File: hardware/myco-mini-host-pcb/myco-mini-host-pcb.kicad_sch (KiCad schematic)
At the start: 38 parts, among them J1 Conn_01x17_Female, J2 Conn_01x17_Female, Q1 AO3401A, Q2 AO3401A, Q3 AO3401A, Q4 AO3401A, SW1 DM-04-V, SW2 TS-1187A-B-A-B, U1 XC9145B33CMR-G, U2 SHT41-AD1B-R2, U3 BH1750FVI-TR, U4 MAX40203AUK+T

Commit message: refactor: echange P1.12/P1.13 entre SENSOR_EN et BAT_SENSE
- SENSOR_EN : P1.12 (J1 pin5) -> P1.13 (J1 pin6)
- BAT_SENSE : P1.13 (J1 pin6) -> P1.12 (J1 pin5)

Verifie avant application : P1.12 = AIN5 et P1.13 = AIN6 dans les tables de
brochage du datasheet nRF54L15, donc les deux broches sont capables SAADC.
L'echange est valide dans les deux sens - BAT_SENSE garde une entree
analogique reelle sur P1.12, et SENSOR_EN n'a besoin que d'un GPIO general.

Nets renommes en consequence (P1_12_SENSOR_EN -> P1_13_SENSOR_EN,
P1_13_BAT_SENSE -> P1_12_BAT_SENSE), plus les notes de Q3/Q4 et la BOM.

Alignement des textes preserve : diff UUID sur les 79 labels, zero
deplacement (7 renommages voulus). ERC inchange a 69.

Co-Authored-By: Claude Sonnet 5 <noreply@anthropic.com>
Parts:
- Q3: Note Sensor VCC switch (BH1750+SHT41+their I2C pull-ups): S=VOUT_3V3 D=SENSOR_3V3 G=P1_12_SENSOR_EN. Added when nRF54 moved onto VOUT_3V3 (was VDD_NRF direct-battery) - sensors need their own switch now to still power down in deep sleep. R1/R2 (I2C pull-ups) moved to SENSOR_3V3 too, so an unpowered sensor isn't backfed through its own SDA/SCL ESD clamps. -> Sensor VCC switch (BH1750+SHT41+their I2C pull-ups): S=VOUT_3V3 D=SENSOR_3V3 G=P1_13_SENSOR_EN. Added when nRF54 moved onto VOUT_3V3 (was VDD_NRF direct-battery) - sensors need their own switch now to still power down in deep sleep. R1/R2 (I2C pull-ups) moved to SENSOR_3V3 too, so an unpowered sensor isn't backfed through its own SDA/SCL ESD clamps.
- Q4: Note Battery-sense divider switch: S=BAT_RAW D=BAT_SENSE_TOP G=P1_12_SENSOR_EN (shared with Q3). Keeps the R11/R12 divider disconnected from BAT_RAW except during the brief active-measurement window, avoiding a continuous leakage path now that the free internal-VDD SAADC battery trick no longer works (VDD_NRF is regulated 3.3V post-merge, not the raw cell). -> Battery-sense divider switch: S=BAT_RAW D=BAT_SENSE_TOP G=P1_13_SENSOR_EN (shared with Q3). Keeps the R11/R12 divider disconnected from BAT_RAW except during the brief active-measurement window, avoiding a continuous leakage path now that the free internal-VDD SAADC battery trick no longer works (VDD_NRF is regulated 3.3V post-merge, not the raw cell).
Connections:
- net P1_12_SENSOR_EN renamed P1_13_SENSOR_EN
- net P1_13_SENSOR_EN: now also J1.6 (Pin_6); no longer J1.5 (Pin_5)
- net P1_13_BAT_SENSE renamed P1_12_BAT_SENSE
- net P1_12_BAT_SENSE: now also J1.5 (Pin_5); no longer J1.6 (Pin_6)
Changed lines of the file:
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@@
 		)
 	)
-	(label "P1_12_SENSOR_EN"
+	(label "P1_13_SENSOR_EN"
 		(at 387.35 90.17 0)
 		(effects
@@
 		)
 	)
-	(label "P1_13_BAT_SENSE"
+	(label "P1_12_BAT_SENSE"
 		(at 412.75 121.92 0)
 		(effects
@@
 		)
 	)
-	(label "P1_13_BAT_SENSE"
+	(label "P1_12_BAT_SENSE"
 		(at 412.75 127 0)
 		(effects
@@
 		)
 	)
-	(label "P1_13_BAT_SENSE"
+	(label "P1_13_SENSOR_EN"
 		(at 46.99 179.07 0)
 		(effects
@@
 		)
 	)
-	(label "P1_12_SENSOR_EN"
+	(label "P1_12_BAT_SENSE"
 		(at 46.99 176.53 0)
 		(effects
@@
 		)
 	)
-	(label "P1_12_SENSOR_EN"
+	(label "P1_13_SENSOR_EN"
 		(at 386.08 44.45 0)
 		(effects
@@
 		)
 	)
-	(label "P1_12_SENSOR_EN"
+	(label "P1_13_SENSOR_EN"
 		(at 264.16 87.63 0)
 		(effects
@@
 			)
 		)
-		(property "Note" "Battery-sense divider switch: S=BAT_RAW D=BAT_SENSE_TOP G=P1_12_SENSOR_EN (shared with Q3). Keeps the R11/R12 divider disconnected from BAT_RAW except during the brief active-measurement window, avoiding a continuous leakage path now that the free internal-VDD SAADC battery trick no longer works (VDD_NRF is regulated 3.3V post-merge, not the raw cell)."
+		(property "Note" "Battery-sense divider switch: S=BAT_RAW D=BAT_SENSE_TOP G=P1_13_SENSOR_EN (shared with Q3). Keeps the R11/R12 divider disconnected from BAT_RAW except during the brief active-measurement window, avoiding a continuous leakage path now that the free internal-VDD SAADC battery trick no longer works (VDD_NRF is regulated 3.3V post-merge, not the raw cell)."
 			(at 410.21 90.17 0)
 			(hide yes)
@@
 			)
 		)
-		(property "Note" "Sensor VCC switch (BH1750+SHT41+their I2C pull-ups): S=VOUT_3V3 D=SENSOR_3V3 G=P1_12_SENSOR_EN. Added when nRF54 moved onto VOUT_3V3 (was VDD_NRF direct-battery) - sensors need their own switch now to still power down in deep sleep. R1/R2 (I2C pull-ups) moved to SENSOR_3V3 too, so an unpowered sensor isn't backfed through its own SDA/SCL ESD clamps."
+		(property "Note" "Sensor VCC switch (BH1750+SHT41+their I2C pull-ups): S=VOUT_3V3 D=SENSOR_3V3 G=P1_13_SENSOR_EN. Added when nRF54 moved onto VOUT_3V3 (was VDD_NRF direct-battery) - sensors need their own switch now to still power down in deep sleep. R1/R2 (I2C pull-ups) moved to SENSOR_3V3 too, so an unpowered sensor isn't backfed through its own SDA/SCL ESD clamps."
 			(at 410.21 44.45 0)
 			(hide yes)

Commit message: feat: C6 (100uF) passe de 0805 a 1206 - moins cher et moins de derating
Le 100uF n'existe qu'en 6.3V en boitier 0805, ce qui en faisait le 3e
composant le plus cher de la carte ($0.63, C141660) pour une capacite
effective fortement reduite par le derating DC bias a 3.3V.

En 1206 : GRM31CR61A107ME05L (Murata, C312983) a $0.3505 (MOQ 5, 81k en
stock) et surtout en 10V au lieu de 6.3V, donc bien moins de derating a
3.3V - on paie moins cher pour plus de capacite reelle.

Empreinte du schema passee a Capacitor_SMD:C_1206_3216Metric (verifie que
les autres condensateurs 0805 ne sont pas affectes). Placement PCB a faire
par l'utilisateur, qui a confirme qu'il y a la place a l'emplacement actuel.

Passifs + inductance : $1.19 -> $0.91/carte.

Co-Authored-By: Claude Sonnet 5 <noreply@anthropic.com>
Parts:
- C6: footprint Capacitor_SMD:C_0805_2012Metric -> Capacitor_SMD:C_1206_3216Metric
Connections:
- no-connect marks 19 -> 21
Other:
- moved on the sheet: SW1

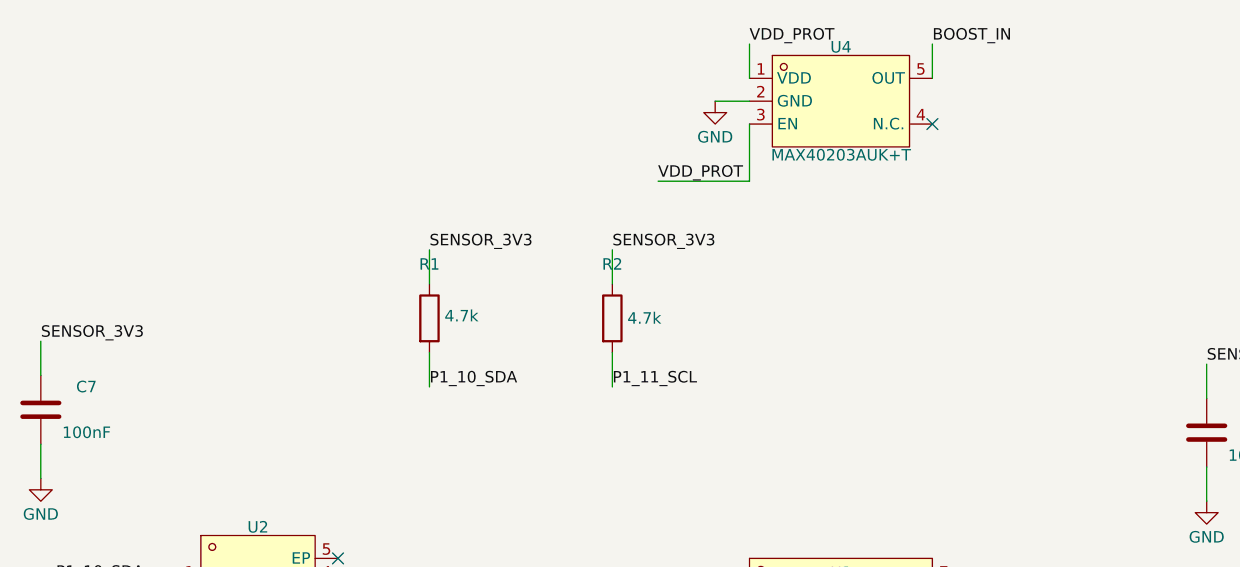
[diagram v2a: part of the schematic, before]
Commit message: fix: types electriques des broches des symboles custom - ERC 56 -> 6
easyeda2kicad laisse toutes les broches en 'unspecified', ce qui rendait
l'ERC inexploitable : 50 des 56 remontees (89%) etaient des avertissements
de compatibilite de types, aucun ne correspondant a un vrai defaut. Un vrai
avertissement pouvait s'y perdre.

Broches typees dans la librairie ET dans le cache lib_symbols du schema
(les deux doivent concorder) :
  power_in      VDD/VCC/VSS/GND/BAT
  power_out     VOUT (U1), OUT (U4)
  input         CE, EN, ADDR, DVI, SCL
  bidirectional SDA
  passive       MOSFET, LED, interrupteurs, sonde sol, pads thermiques, LX

Deux PWR_FLAG ajoutes (#FLG02 sur SENSOR_3V3, #FLG03 sur VDD_PROT) : ces
rails sont alimentes a travers un MOSFET, dont les broches sont 'passive',
donc KiCad n'y voyait aucune source et signalait 'Input Power pin not driven'.
Reference masquee sur les deux (convention, et evite un chevauchement de
texte avec les labels).

Bug corrige en cours de route : la premiere version du script ne
reinitialisait pas le symbole courant en entrant dans un symbole hors table,
et a donc retype les broches de power:GND, power:PWR_FLAG et Device:R/C -
16 erreurs 'Pin not connected' sont apparues. Detecte par l'ERC, restaure
depuis snapshot, corrige, verifie que les symboles stock gardent bien
power_in / power_out / passive.

Resultat : ERC 56 -> 6, dont ZERO erreur. Restent 3 off-grid (edition
manuelle de la zone SW1) et 3 'doesn't match copy in library' (cosmetique,
disparait via 'Update Symbol from Library' dans KiCad).

Connectivite verifiee identique net par net (hors les 2 PWR_FLAG).
Alignement des textes preserve : diff UUID sur 79 labels, zero deplacement.

Co-Authored-By: Claude Sonnet 5 <noreply@anthropic.com>
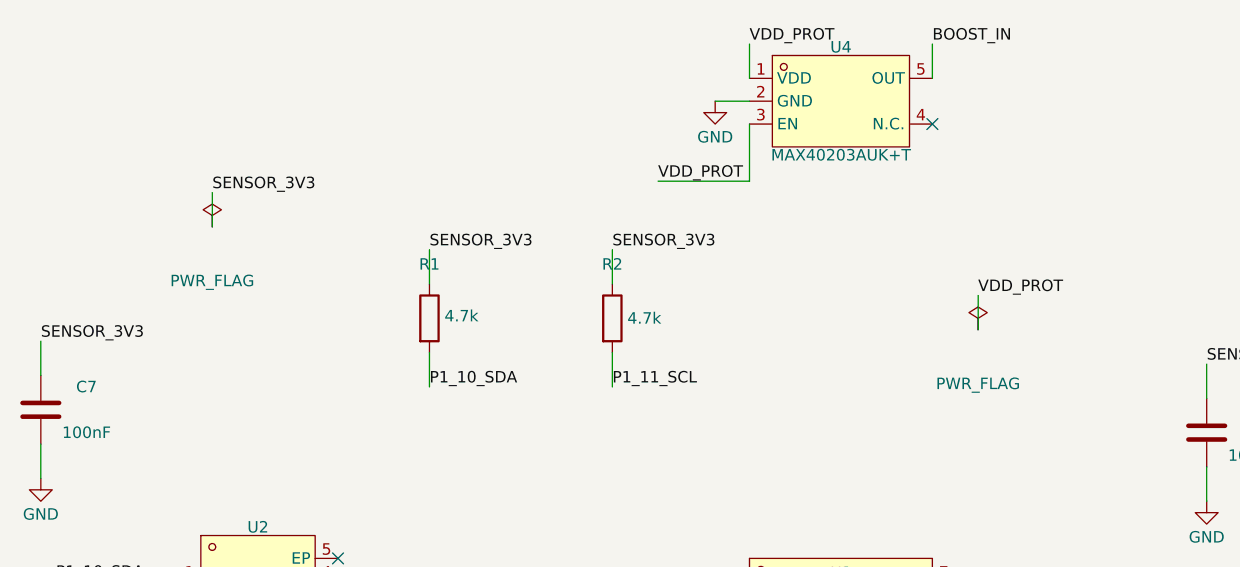
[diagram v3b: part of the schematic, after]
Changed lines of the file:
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@@
 	(wire
 		(pts
-			(xy 97.79 129.54) (xy 101.6 129.54)
-		)
-		(stroke
-			(width 0)
-			(type default)
-		)
-	)
-	(wire
-		(pts
 			(xy 337.82 217.17) (xy 341.63 217.17)
 		)
@@
 		)
 	)
+	(wire
+		(pts
+			(xy 97.79 129.54) (xy 101.6 129.54)
+		)
+		(stroke
+			(width 0)
+			(type default)
+		)
+	)
+	(wire
+		(pts
+			(xy 105.41 90.17) (xy 105.41 86.36)
+		)
+		(stroke
+			(width 0)
+			(type default)
+		)
+	)
+	(wire
+		(pts
+			(xy 190.5 101.6) (xy 190.5 97.78999999999999)
+		)
+		(stroke
+			(width 0)
+			(type default)
+		)
+	)
 	(label "SENSOR_3V3"
 		(at 129.54 92.71 0)
@@
 		)
 	)
+	(label "SENSOR_3V3"
+		(at 105.41 86.36 0)
+		(effects
+			(font
+				(size 1.27 1.27)
+			)
+			(justify left bottom)
+		)
+	)
+	(label "VDD_PROT"
+		(at 190.5 97.78999999999999 0)
+		(effects
+			(font
+				(size 1.27 1.27)
+			)
+			(justify left bottom)
+		)
+	)
 	(symbol
 		(lib_id "power:GND")
@@
 					(unit 1)
 				)
+			)
+		)
+	)
+	(symbol
+		(lib_id "power:PWR_FLAG")
+		(at 105.41 90.17 0)
+		(unit 1)
+		(body_style 1)
+		(exclude_from_sim no)
+		(in_bom no)
+		(on_board yes)
+		(in_pos_files yes)
+		(dnp no)
+		(property "Reference" "#FLG02"
+			(at 105.41 84.17 0)
+			(hide yes)
+			(show_name no)
+			(do_not_autoplace no)
+			(effects
+				(font
+					(size 1.27 1.27)
+				)
+			)
+		)
+		(property "Value" "PWR_FLAG"
+			(at 105.41 96.17 0)
+			(show_name no)
+			(do_not_autoplace no)
+			(effects
+				(font
+					(size 1.27 1.27)
+				)
+			)
+		)
+		(property "Footprint" ""
+			(at 105.41 90.17 0)
+			(hide yes)
+			(show_name no)
+			(do_not_autoplace no)
+			(effects
+				(font
+					(size 1.27 1.27)
+				)
+			)
+		)
+		(property "Datasheet" ""
+			(at 105.41 90.17 0)
+			(show_name no)
+			(do_not_autoplace no)
+			(effects
+				(font
+					(size 1.27 1.27)
+				)
+			)
+		)
+		(property "Description" ""
+			(at 105.41 90.17 0)
+			(show_name no)
+			(do_not_autoplace no)
+			(effects
+				(font
+					(size 1.27 1.27)
+				)
+			)
+		)
+		(pin "1"
+		)
+		(instances
+			(project "myco-mini-host-pcb"
+				(path "/b1969cb4-f84b-4d7e-8508-ab863aa656b2"
+					(reference "#FLG02")
+					(unit 1)
+				)
+			)
+		)
+	)
+	(symbol
+		(lib_id "power:PWR_FLAG")
+		(at 190.5 101.6 0)
+		(unit 1)
+		(body_style 1)
+		(exclude_from_sim no)
+		(in_bom no)
+		(on_board yes)
+		(in_pos_files yes)
+		(dnp no)
+		(property "Reference" "#FLG03"
+			(at 190.5 95.6 0)
+			(hide yes)
+			(show_name no)
+			(do_not_autoplace no)
+			(effects
+				(font
+					(size 1.27 1.27)
+				)
+			)
+		)
+		(property "Value" "PWR_FLAG"
+			(at 190.5 107.6 0)
+			(show_name no)
+			(do_not_autoplace no)
+			(effects
+				(font
+					(size 1.27 1.27)
+				)
+			)
+		)
+		(property "Footprint" ""
+			(at 190.5 101.6 0)
+			(hide yes)
+			(show_name no)
+			(do_not_autoplace no)
+			(effects
+				(font
+					(size 1.27 1.27)
+				)
+			)
+		)
+		(property "Datasheet" ""
+			(at 190.5 101.6 0)
+			(show_name no)
+			(do_not_autoplace no)
+			(effects
+				(font
+					(size 1.27 1.27)
+				)
+			)
+		)
+		(property "Description" ""
+			(at 190.5 101.6 0)
+			(show_name no)
+			(do_not_autoplace no)
+			(effects
+				(font
+					(size 1.27 1.27)
+				)
+			)
+		)
+		(pin "1"
+		)
+		(instances
+			(project "myco-mini-host-pcb"
+				(path "/b1969cb4-f84b-4d7e-8508-ab863aa656b2"
+					(reference "#FLG03")
+					(unit 1)
+				)

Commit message: feat: v1.0.0 - host PCB routé, DRC clean, prêt fab JLCPCB
- Routage complet par l'utilisateur (placement, guard zone soil probe,
  teardrops, trou de fixation gauche)
- Corrections issues de la review Opus 5 finale : dimensions du slit
  d'isolation thermique U2 mises à la spec (1.05mm uniforme sur les
  3 bras), pastilles paste/mask retirées sur U2 (SHT40) et U3 (BH1750)
  pour leurs pads die-exposée, resync librairie<->instances PCB
  (SW1 modèle 3D, BT1 attr smd, courtoisies F.CrtYd manquantes sur
  SW1/SW2/U4)
- 3 vias de la sonde sol passés en plugged+capped (IPC-4761)
- BOM : références LCSC vérifiées et prix réels pour tous les passifs
- DRC final : 0 violation, 0 unconnected
- Ajout docs/cost-tracking.md (suivi des coûts réels host PCB +
  breakout + composants, synchronisé sur le wiki GitHub)
- Datasheets BH1750 et Sensirion (SHT4x) ajoutés à misc/
- .gitignore : exclusion des exports générés (gerbers JLCPCB, rendus
  SVG temporaires) qui ne sont pas du code source

Co-Authored-By: Claude Sonnet 5 <noreply@anthropic.com>
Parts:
- removed C6: 100uF, Capacitor_SMD:C_1206_3216Metric, symbol Device:C
- removed Q2: AO3401A, myco_host:SOT-23_L2.9-W1.3-P1.90-LS2.4-BR, symbol myco_host:AO3401A
- removed R5: 100k, Resistor_SMD:R_0603_1608Metric, symbol Device:R
- added C10: 100nF, Capacitor_SMD:C_0603_1608Metric, symbol Device:C
- C7: Note Local bypass at U2 (SHT41). SENSOR_3V3 decoupling. The rail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 -> Local bypass at U2 (SHT40). SENSOR_3V3 decoupling. The rail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
- L1: Note Shielded inductor recommended (datasheet note) -> Swapped 2026-08-24: TDK MLP2520S4R7ST0S1 (C383386) -> TDK T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
- Q3: Note Sensor VCC switch (BH1750+SHT41+their I2C pull-ups): S=VOUT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 -> Sensor VCC switch (BH1750+SHT40+their I2C pull-ups): S=VOUT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
- SW1: LCSC Part (none) -> C501537; Note Swapped from EM-04-Q (out of stock at LCSC as of 2026-08-22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 -> SW1 (EM-04-Q) alternative - out of stock at LCSC as of 2026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
- U2: value SHT41-AD1B-R2 -> SHT40-AD1B-R2; symbol myco_host:SHT41-AD1B-R2 -> myco_host:SHT40-AD1B-R2; LCSC C7461861 -> C2909890; LCSC Part C7461861 -> C2909890; Note Same DFN-4 1.5x1.5mm package/pinout as SHT40, better accura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 -> Reverted to SHT40 on 2026-08-24. Identical DFN-4 1.5x1.5mm 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
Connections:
- net SOIL_VCC is gone; now on net P1_08_SOIL_SW: R3.1, R4.1
- net GND: now also C10.2
- net SENSOR_3V3: no longer U3.5 (DVI)
- net P1_14_SENSOR_EN: now reaches J1.7 (Pin_7)
- net P1_14_SENSOR_EN: now also Q3.1 (G), Q4.1 (G), R13.2
- net P1_12_BAT_SENSE renamed P1_13_BAT_SENSE
- net P1_13_BAT_SENSE: now also J1.6 (Pin_6); no longer J1.5 (Pin_5)
- removed net P1_13_SENSOR_EN: J1.6 (Pin_6), Q3.1 (G), Q4.1 (G), R13.2
- new net P1_12_BH_DVI: C10.1, J1.5 (Pin_5), U3.5 (DVI)
- no-connect marks 21 -> 20
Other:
- note added: "Battery Sensor"
- note added: "Power Rail"
- note added: "Sensors power control"
- note added: "Socket for Custom AN54LV15 breakout board"
- note removed: "Myco Mini - Host PCB (proto validation) - Premier jet, non revise - voir docs/pcb-design-decisions.md"
- moved on the sheet: BT1, C1, C2, C3, C4, C5, C7, C8, C9, D1, J1, J2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
